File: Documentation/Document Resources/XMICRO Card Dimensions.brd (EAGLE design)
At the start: 242.9 x 109.2 mm, 1 part

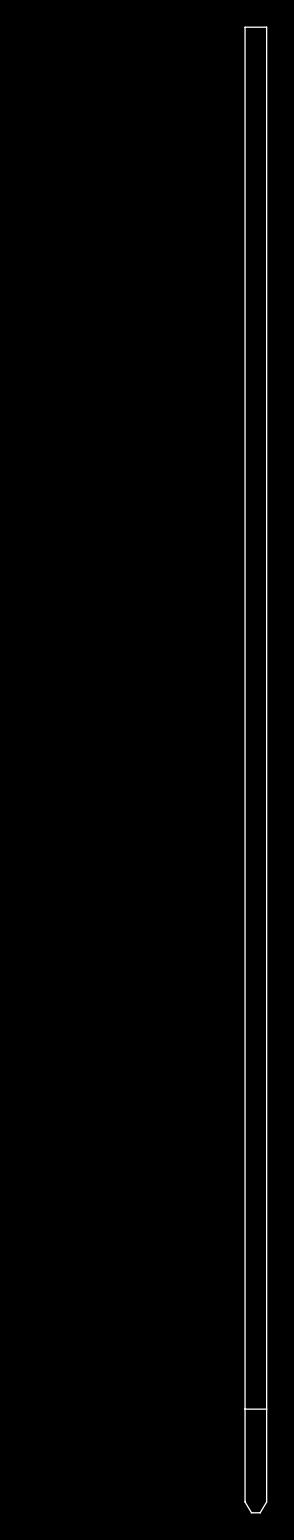
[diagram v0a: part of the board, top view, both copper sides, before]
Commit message: Added backplane dimensions and updated the specification document
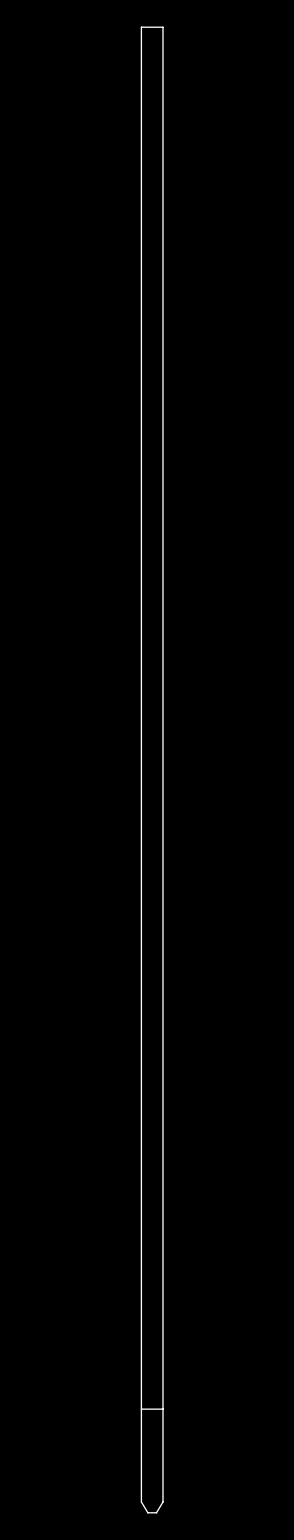
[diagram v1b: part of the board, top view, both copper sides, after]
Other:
- board size 242.9 x 109.2 mm -> 235.3 x 109.2 mm
- board text added: "0.2" TO OUTSIDE OF CHASSIS"
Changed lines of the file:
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@@
 <layer number="14" name="Route14" color="1" fill="6" visible="no" active="no"/>
 <layer number="15" name="Route15" color="4" fill="6" visible="no" active="no"/>
-<layer number="16" name="Bottom" color="1" fill="1" visible="no" active="yes"/>
+<layer number="16" name="Bottom" color="1" fill="1" visible="yes" active="yes"/>
 <layer number="17" name="Pads" color="2" fill="1" visible="yes" active="yes"/>
 <layer number="18" name="Vias" color="2" fill="1" visible="yes" active="yes"/>
@@
 </polygon>
 <text x="177.8" y="20.32" size="2.1844" layer="51" font="vector" align="bottom-center">2" TO CONNECTOR CENTER</text>
-<wire x1="101.6" y1="101.6" x2="101.6" y2="0" width="0.0635" layer="51" style="shortdash"/>
+<wire x1="101.6" y1="101.6" x2="101.6" y2="0" width="0.0635" layer="51" style="longdash"/>
 <wire x1="203.2" y1="106.68" x2="101.6" y2="106.68" width="0.0635" layer="51"/>
 <wire x1="101.6" y1="104.14" x2="101.6" y2="106.68" width="0.0635" layer="51"/>
@@
 <vertex x="199.54875" y="55.40375"/>
 </polygon>
-<wire x1="241.77625" y1="-7.62" x2="241.3" y2="-6.82625" width="0" layer="20"/>
-<wire x1="241.3" y1="-6.82625" x2="241.3" y2="0" width="0" layer="20"/>
-<wire x1="241.3" y1="0" x2="241.3" y2="101.6" width="0" layer="20"/>
-<wire x1="242.41125" y1="-7.62" x2="242.8875" y2="-6.82625" width="0" layer="20"/>
-<wire x1="242.8875" y1="-6.82625" x2="242.8875" y2="0" width="0" layer="20"/>
-<wire x1="242.8875" y1="0" x2="242.8875" y2="101.6" width="0" layer="20"/>
-<wire x1="241.3" y1="101.6" x2="242.8875" y2="101.6" width="0" layer="20"/>
-<wire x1="241.77625" y1="-7.62" x2="242.41125" y2="-7.62" width="0" layer="20"/>
-<wire x1="241.3" y1="109.22" x2="241.3" y2="106.68" width="0.0635" layer="51"/>
-<wire x1="241.3" y1="106.68" x2="241.3" y2="104.14" width="0.0635" layer="51"/>
-<wire x1="242.8875" y1="104.14" x2="242.8875" y2="106.68" width="0.0635" layer="51"/>
-<polygon width="0.0635" layer="51">
-<vertex x="241.3" y="106.68"/>
-<vertex x="240.18875" y="107.15625"/>
-<vertex x="240.18875" y="106.20375"/>
-</polygon>
-<polygon width="0.0635" layer="51">
-<vertex x="242.8875" y="106.68"/>
-<vertex x="243.99875" y="106.20375"/>
-<vertex x="243.99875" y="107.15625"/>
-</polygon>
-<wire x1="242.8875" y1="106.68" x2="242.8875" y2="109.22" width="0.0635" layer="51"/>
-<wire x1="241.3" y1="106.68" x2="238.76" y2="106.68" width="0.0635" layer="51"/>
-<wire x1="242.8875" y1="106.68" x2="245.4275" y2="106.68" width="0.0635" layer="51"/>
-<text x="246.38" y="106.68" size="2.1844" layer="51" font="vector" align="center-left">0.0625"</text>
-<wire x1="238.76" y1="88.9" x2="238.76" y2="86.36" width="0.0635" layer="51"/>
-<polygon width="0.0635" layer="51">
-<vertex x="238.76" y="86.36"/>
-<vertex x="239.87125" y="85.88375"/>
-<vertex x="239.87125" y="86.83625"/>
-</polygon>
-<wire x1="238.76" y1="86.36" x2="238.76" y2="83.82" width="0.0635" layer="51"/>
-<wire x1="238.76" y1="86.36" x2="241.3" y2="86.36" width="0.0635" layer="51"/>
-<text x="245.4275" y="50.8" size="3.81" layer="51" font="vector" rot="R90" align="top-center">COMPONENT SIDE</text>
-<text x="236.22" y="86.36" size="2.1844" layer="51" font="vector" rot="R90" align="bottom-center">0.1" MAXIMUM
+<wire x1="234.15625" y1="-7.62" x2="233.68" y2="-6.82625" width="0" layer="20"/>
+<wire x1="233.68" y1="-6.82625" x2="233.68" y2="0" width="0" layer="20"/>
+<wire x1="233.68" y1="0" x2="233.68" y2="101.6" width="0" layer="20"/>
+<wire x1="234.79125" y1="-7.62" x2="235.2675" y2="-6.82625" width="0" layer="20"/>
+<wire x1="235.2675" y1="-6.82625" x2="235.2675" y2="0" width="0" layer="20"/>
+<wire x1="235.2675" y1="0" x2="235.2675" y2="101.6" width="0" layer="20"/>
+<wire x1="233.68" y1="101.6" x2="235.2675" y2="101.6" width="0" layer="20"/>
+<wire x1="234.15625" y1="-7.62" x2="234.79125" y2="-7.62" width="0" layer="20"/>
+<wire x1="233.68" y1="109.22" x2="233.68" y2="106.68" width="0.0635" layer="51"/>
+<wire x1="233.68" y1="106.68" x2="233.68" y2="104.14" width="0.0635" layer="51"/>
+<wire x1="235.2675" y1="104.14" x2="235.2675" y2="106.68" width="0.0635" layer="51"/>
+<polygon width="0.0635" layer="51">
+<vertex x="233.68" y="106.68"/>
+<vertex x="232.56875" y="107.15625"/>
+<vertex x="232.56875" y="106.20375"/>
+</polygon>
+<polygon width="0.0635" layer="51">
+<vertex x="235.2675" y="106.68"/>
+<vertex x="236.37875" y="106.20375"/>
+<vertex x="236.37875" y="107.15625"/>
+</polygon>
+<wire x1="235.2675" y1="106.68" x2="235.2675" y2="109.22" width="0.0635" layer="51"/>
+<wire x1="233.68" y1="106.68" x2="231.14" y2="106.68" width="0.0635" layer="51"/>
+<wire x1="235.2675" y1="106.68" x2="237.8075" y2="106.68" width="0.0635" layer="51"/>
+<text x="238.76" y="106.68" size="2.1844" layer="51" font="vector" align="center-left">0.0625"</text>
+<wire x1="231.14" y1="88.9" x2="231.14" y2="86.36" width="0.0635" layer="51"/>
+<polygon width="0.0635" layer="51">
+<vertex x="231.14" y="86.36"/>
+<vertex x="232.25125" y="85.88375"/>
+<vertex x="232.25125" y="86.83625"/>
+</polygon>
+<wire x1="231.14" y1="86.36" x2="231.14" y2="83.82" width="0.0635" layer="51"/>
+<wire x1="231.14" y1="86.36" x2="233.68" y2="86.36" width="0.0635" layer="51"/>
+<text x="237.8075" y="50.8" size="3.81" layer="51" font="vector" rot="R90" align="top-center">COMPONENT SIDE</text>
+<text x="228.6" y="86.36" size="2.1844" layer="51" font="vector" rot="R90" align="bottom-center">0.1" MAXIMUM
  BOTTOM HEIGHT</text>
-<wire x1="257.81" y1="83.82" x2="257.81" y2="86.36" width="0.0635" layer="51"/>
-<polygon width="0.0635" layer="51">
-<vertex x="257.81" y="86.36"/>
-<vertex x="256.69875" y="86.83625"/>
-<vertex x="256.69875" y="85.88375"/>
-</polygon>
-<wire x1="257.81" y1="86.36" x2="257.81" y2="88.9" width="0.0635" layer="51"/>
-<wire x1="257.81" y1="86.36" x2="242.8875" y2="86.36" width="0.0635" layer="51"/>
-<text x="260.35" y="86.36" size="2.1844" layer="51" font="vector" rot="R90" align="top-center">0.5875" MAXIMUM
+<wire x1="250.19" y1="83.82" x2="250.19" y2="86.36" width="0.0635" layer="51"/>
+<polygon width="0.0635" layer="51">
+<vertex x="250.19" y="86.36"/>
+<vertex x="249.07875" y="86.83625"/>
+<vertex x="249.07875" y="85.88375"/>
+</polygon>
+<wire x1="250.19" y1="86.36" x2="250.19" y2="88.9" width="0.0635" layer="51"/>
+<wire x1="250.19" y1="86.36" x2="235.2675" y2="86.36" width="0.0635" layer="51"/>
+<text x="252.73" y="86.36" size="2.1844" layer="51" font="vector" rot="R90" align="top-center">0.5875" MAXIMUM
 TOP HEIGHT</text>
 <polygon width="0.0635" layer="51">
-<vertex x="242.8875" y="86.36"/>
-<vertex x="243.99875" y="85.88375"/>
-<vertex x="243.99875" y="86.83625"/>
-</polygon>
-<wire x1="241.3" y1="0" x2="242.8875" y2="0" width="0" layer="20"/>
-<text x="266.7" y="-33.02" size="5.08" layer="51" font="vector" ratio="10" align="bottom-right">XMICRO CARD DIMENSIONS</text>
-<text x="266.7" y="-38.1" size="2.54" layer="51" font="vector" ratio="10" align="bottom-right">V1.0 2018-10-07</text>
-<text x="250.5075" y="50.8" size="1.6764" layer="51" font="vector" rot="R90" align="top-center">VIEWED FROM FRONT EDGE</text>
+<vertex x="235.2675" y="86.36"/>
+<vertex x="236.37875" y="85.88375"/>
+<vertex x="236.37875" y="86.83625"/>
+</polygon>
+<wire x1="233.68" y1="0" x2="235.2675" y2="0" width="0" layer="20"/>
+<text x="259.08" y="-33.02" size="5.08" layer="51" font="vector" ratio="10" align="bottom-right">XMICRO CARD DIMENSIONS</text>
+<text x="259.08" y="-38.1" size="2.54" layer="51" font="vector" ratio="10" align="bottom-right">V1.0 2018-10-07</text>
+<text x="242.8875" y="50.8" size="1.6764" layer="51" font="vector" rot="R90" align="top-center">VIEWED FROM FRONT EDGE</text>
+<wire x1="208.28" y1="116.84" x2="208.28" y2="104.14" width="0" layer="51" style="shortdash"/>
+<wire x1="203.2" y1="114.3" x2="208.28" y2="114.3" width="0.0635" layer="51"/>
+<polygon width="0.0635" layer="51">
+<vertex x="203.2" y="114.3"/>
+<vertex x="204.31125" y="113.82375"/>
+<vertex x="204.31125" y="114.77625"/>
+</polygon>
+<polygon width="0.0635" layer="51">
+<vertex x="208.28" y="114.3"/>
+<vertex x="207.16875" y="114.77625"/>
+<vertex x="207.16875" y="113.82375"/>
+</polygon>
+<text x="205.74" y="119.38" size="2.1844" layer="51" font="vector" align="bottom-center">0.2" TO OUTSIDE
+OF CHASSIS</text>
 </plain>
 <attributes>

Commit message: Updated specification document and dimensional drawings
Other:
- board text removed: "V1.0 2018-10-07"
- board text removed: "XMICRO CARD DIMENSIONS"
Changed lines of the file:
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@@
 <setting verticaltext="up"/>
 </settings>
-<grid distance="0.1" unitdist="inch" unit="inch" style="dots" multiple="1" display="no" altdistance="0.00625" altunitdist="inch" altunit="inch"/>
+<grid distance="0.1" unitdist="inch" unit="inch" style="dots" multiple="1" display="no" altdistance="0.05" altunitdist="inch" altunit="inch"/>
 <layers>
 <layer number="1" name="Top" color="4" fill="1" visible="yes" active="yes"/>
@@
 PAD</text>
 <text x="116.84" y="2.54" size="2.1844" layer="51" font="vector" align="center-left">PIN 1</text>
-<text x="0" y="-38.1" size="1.6764" layer="51" font="vector">NOTES:
+<text x="0" y="-5.08" size="1.6764" layer="51" font="vector" align="top-left">NOTES:
 1. All dimensions are in inches.
 2. Mounting holes should be plated through and tied to system GND
@@
 <polygon width="0.0635" layer="51">
 <vertex x="231.14" y="86.36"/>
-<vertex x="232.25125" y="85.88375"/>
-<vertex x="232.25125" y="86.83625"/>
+<vertex x="231.93375" y="85.88375"/>
+<vertex x="231.93375" y="86.83625"/>
 </polygon>
 <wire x1="231.14" y1="86.36" x2="231.14" y2="83.82" width="0.0635" layer="51"/>
@@
 </polygon>
 <wire x1="233.68" y1="0" x2="235.2675" y2="0" width="0" layer="20"/>
-<text x="259.08" y="-33.02" size="5.08" layer="51" font="vector" ratio="10" align="bottom-right">XMICRO CARD DIMENSIONS</text>
-<text x="259.08" y="-38.1" size="2.54" layer="51" font="vector" ratio="10" align="bottom-right">V1.0 2018-10-07</text>
 <text x="242.8875" y="50.8" size="1.6764" layer="51" font="vector" rot="R90" align="top-center">VIEWED FROM FRONT EDGE</text>
 <wire x1="208.28" y1="116.84" x2="208.28" y2="104.14" width="0" layer="51" style="shortdash"/>
@@
 <text x="205.74" y="119.38" size="2.1844" layer="51" font="vector" align="bottom-center">0.2" TO OUTSIDE
 OF CHASSIS</text>
+<polygon width="0.0635" layer="51">
+<vertex x="233.68" y="86.36"/>
+<vertex x="232.88625" y="86.83625"/>
+<vertex x="232.88625" y="85.88375"/>
+</polygon>
 </plain>
 <attributes>

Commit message: Updated physical dimensions (PCB rear edge to chassis)
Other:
- board text added: "0.1" TO INSIDE SURFACE OF CHASSIS"
- board text removed: "0.2" TO OUTSIDE OF CHASSIS"
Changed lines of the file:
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@@
 <setting verticaltext="up"/>
 </settings>
-<grid distance="0.1" unitdist="inch" unit="inch" style="dots" multiple="1" display="no" altdistance="0.05" altunitdist="inch" altunit="inch"/>
+<grid distance="0.1" unitdist="inch" unit="inch" style="dots" multiple="1" display="no" altdistance="0.0125" altunitdist="inch" altunit="inch"/>
 <layers>
 <layer number="1" name="Top" color="4" fill="1" visible="yes" active="yes"/>
@@
 </polygon>
 <text x="101.6" y="50.8" size="3.81" layer="51" font="vector" align="center">COMPONENT SIDE</text>
-<wire x1="205.74" y1="101.6" x2="208.28" y2="101.6" width="0.0635" layer="51"/>
-<wire x1="208.28" y1="101.6" x2="210.82" y2="101.6" width="0.0635" layer="51"/>
-<wire x1="208.28" y1="101.6" x2="208.28" y2="0" width="0.0635" layer="51"/>
-<wire x1="205.74" y1="0" x2="208.28" y2="0" width="0.0635" layer="51"/>
-<wire x1="208.28" y1="0" x2="210.82" y2="0" width="0.0635" layer="51"/>
-<wire x1="208.28" y1="0" x2="208.28" y2="-7.62" width="0.0635" layer="51"/>
-<wire x1="195.58" y1="-7.62" x2="210.82" y2="-7.62" width="0.0635" layer="51"/>
-<text x="210.82" y="50.8" size="2.1844" layer="51" font="vector" align="center-left">4"</text>
-<text x="210.82" y="-3.81" size="2.1844" layer="51" font="vector" align="center-left">0.3"</text>
+<wire x1="209.55" y1="101.6" x2="210.82" y2="101.6" width="0.0635" layer="51"/>
+<wire x1="210.82" y1="101.6" x2="213.36" y2="101.6" width="0.0635" layer="51"/>
+<wire x1="210.82" y1="101.6" x2="210.82" y2="0" width="0.0635" layer="51"/>
+<wire x1="209.55" y1="0" x2="210.82" y2="0" width="0.0635" layer="51"/>
+<wire x1="210.82" y1="0" x2="213.36" y2="0" width="0.0635" layer="51"/>
+<wire x1="210.82" y1="0" x2="210.82" y2="-7.62" width="0.0635" layer="51"/>
+<wire x1="195.58" y1="-7.62" x2="213.36" y2="-7.62" width="0.0635" layer="51"/>
+<text x="213.36" y="50.8" size="2.1844" layer="51" font="vector" align="center-left">4"</text>
+<text x="213.36" y="-3.81" size="2.1844" layer="51" font="vector" align="center-left">0.3"</text>
 <wire x1="193.04" y1="-10.16" x2="193.04" y2="-12.7" width="0.0635" layer="51"/>
 <wire x1="193.04" y1="-12.7" x2="193.04" y2="-15.24" width="0.0635" layer="51"/>
@@
 </polygon>
 <polygon width="0.0635" layer="51">
-<vertex x="208.28" y="-7.62"/>
-<vertex x="208.75625" y="-6.50875"/>
-<vertex x="207.80375" y="-6.50875"/>
-</polygon>
-<polygon width="0.0635" layer="51">
-<vertex x="208.28" y="0"/>
-<vertex x="207.80375" y="-1.11125"/>
-<vertex x="208.75625" y="-1.11125"/>
-</polygon>
-<polygon width="0.0635" layer="51">
-<vertex x="208.28" y="0"/>
-<vertex x="208.75625" y="1.11125"/>
-<vertex x="207.80375" y="1.11125"/>
-</polygon>
-<polygon width="0.0635" layer="51">
-<vertex x="208.28" y="101.6"/>
-<vertex x="207.80375" y="100.48875"/>
-<vertex x="208.75625" y="100.48875"/>
+<vertex x="210.82" y="-7.62"/>
+<vertex x="211.29625" y="-6.50875"/>
+<vertex x="210.34375" y="-6.50875"/>
+</polygon>
+<polygon width="0.0635" layer="51">
+<vertex x="210.82" y="0"/>
+<vertex x="210.34375" y="-1.11125"/>
+<vertex x="211.29625" y="-1.11125"/>
+</polygon>
+<polygon width="0.0635" layer="51">
+<vertex x="210.82" y="0"/>
+<vertex x="211.29625" y="1.11125"/>
+<vertex x="210.34375" y="1.11125"/>
+</polygon>
+<polygon width="0.0635" layer="51">
+<vertex x="210.82" y="101.6"/>
+<vertex x="210.34375" y="100.48875"/>
+<vertex x="211.29625" y="100.48875"/>
 </polygon>
 <wire x1="203.2" y1="104.14" x2="203.2" y2="106.68" width="0.0635" layer="51"/>
@@
 <wire x1="233.68" y1="0" x2="235.2675" y2="0" width="0" layer="20"/>
 <text x="242.8875" y="50.8" size="1.6764" layer="51" font="vector" rot="R90" align="top-center">VIEWED FROM FRONT EDGE</text>
-<wire x1="208.28" y1="116.84" x2="208.28" y2="104.14" width="0" layer="51" style="shortdash"/>
-<wire x1="203.2" y1="114.3" x2="208.28" y2="114.3" width="0.0635" layer="51"/>
+<wire x1="205.74" y1="116.84" x2="205.74" y2="0" width="0" layer="51" style="shortdash"/>
+<wire x1="203.2" y1="114.3" x2="205.74" y2="114.3" width="0.0635" layer="51"/>
 <polygon width="0.0635" layer="51">
 <vertex x="203.2" y="114.3"/>
-<vertex x="204.31125" y="113.82375"/>
-<vertex x="204.31125" y="114.77625"/>
-</polygon>
-<polygon width="0.0635" layer="51">
-<vertex x="208.28" y="114.3"/>
-<vertex x="207.16875" y="114.77625"/>
-<vertex x="207.16875" y="113.82375"/>
-</polygon>
-<text x="205.74" y="119.38" size="2.1844" layer="51" font="vector" align="bottom-center">0.2" TO OUTSIDE
-OF CHASSIS</text>
+<vertex x="203.99375" y="113.82375"/>
+<vertex x="203.99375" y="114.77625"/>
+</polygon>
+<polygon width="0.0635" layer="51">
+<vertex x="205.74" y="114.3"/>
+<vertex x="204.94625" y="114.77625"/>
+<vertex x="204.94625" y="113.82375"/>
+</polygon>
+<text x="204.47" y="119.38" size="2.1844" layer="51" font="vector" align="bottom-center">0.1" TO INSIDE
+SURFACE OF CHASSIS</text>
 <polygon width="0.0635" layer="51">
 <vertex x="233.68" y="86.36"/>

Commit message: Fixed dimensional drawings and pinout diagram
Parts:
- removed PC0: XMICRO-BUS-EDGE62M, Custom:EDGE62M
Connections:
- removed net !BUSACK: PC0.20
- removed net !BUSRQ: PC0.10
- removed net !CBR: PC0.12
- removed net !CINH: PC0.13
- removed net !CSX: PC0.9
- removed net !FETCH: PC0.19
- removed net !HALT: PC0.17
- removed net !INH: PC0.11
- removed net !INT: PC0.51
- removed net !IRQ0: PC0.53
- removed net !IRQ1: PC0.54
- removed net !IRQ2: PC0.55
- removed net !IRQ3: PC0.56
- removed net !IRQ4: PC0.57
- removed net !IRQ5: PC0.58
- removed net !IRQ6: PC0.59
- removed net !IRQ7: PC0.60
- removed net !IRQX: PC0.52
- removed net !NMI: PC0.61
- removed net !RD: PC0.21
- removed net !RST: PC0.14
- removed net !WAIT: PC0.18
- removed net !WR: PC0.22
- removed net +12V: PC0.1
- removed net +3.3V: PC0.2
- removed net +5V: PC0.5, PC0.6
- removed net +5VSB: PC0.8
- removed net -12V: PC0.7
- removed net A0: PC0.23
- removed net A1: PC0.24
- removed net A10: PC0.33
- removed net A11: PC0.34
- removed net A12: PC0.35
- removed net A13: PC0.36
- removed net A14: PC0.37
- removed net A15: PC0.38
- removed net A16: PC0.39
- removed net A17: PC0.40
- removed net A18: PC0.41
- removed net A19: PC0.42
- removed net A2: PC0.25
- removed net A3: PC0.26
- removed net A4: PC0.27
- removed net A5: PC0.28
- removed net A6: PC0.29
- removed net A7: PC0.30
- removed net A8: PC0.31
- removed net A9: PC0.32
- removed net CLK: PC0.15
- removed net CLKAUX: PC0.16
- removed net D0: PC0.43
- removed net D1: PC0.44
- removed net D2: PC0.45
- removed net D3: PC0.46
- removed net D4: PC0.47
- removed net D5: PC0.48
- removed net D6: PC0.49
- removed net D7: PC0.50
- removed net GND: PC0.3, PC0.4, PC0.62
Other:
- board size 235.3 x 109.2 mm -> 228.6 x 109.2 mm
- board text added: "NOTES: 1. All dimensions are in inches. 2. Mounting holes should be plated through and tied to system GND 3. Omit center mounting holes on full-size cards 4. Card edge dimensions according to TE Connectivity 7-5530843-0 5. I/O connectors may only be placed on the rear edge. 6. Other edges require 0.05" component clearence. 7. Pin 1 must be marked."
- board text removed: "NOTES: 1. All dimensions are in inches. 2. Mounting holes should be plated through and tied to system GND 3. Omit center mounting holes on full-size cards 4. Card edge dimensions according to TE Connectivity 7-5530843-0 5. I/O connectors may only be placed on the rear edge. 6. Other edges require 0.05" component clearence."
- board text removed: "VIEWED FROM FRONT EDGE"
